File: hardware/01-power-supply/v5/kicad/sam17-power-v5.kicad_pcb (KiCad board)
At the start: 2 copper layers, 200 x 150 mm, 161 parts, among them J1 KPJX-PM-4S, J10 PinHeader 1x04 P2.54mm, J2 Molex KK-254 4 pos (con llave), J5 Faston 6.3x0.8 PCB, J6 Molex KK-254 2 pos, J8 PinHeader 1x04 P2.54mm, J9 Molex KK-254 2 pos, Q2 N-MOSFET 60V 40A Ron<5mohm, SW1 Pulsador tactil 6x6mm THT, U1 Linear Tech LT1963AEST#TRPBF, U10 TI ADS1115IDGSR, U11 TI TMP1075DGKR, U12 TI INA226AIDGSR, U13 TI INA226AIDGSR, U14 TI INA226AIDGSR, U15 TI LM74502DDFR, U16 TI TPS26630PWPR, U17 TI MSP430FR2111IPW16, U18 TI TPS70933DBVR, U19 TI TPS26630PWPR, U2 Linear Tech LT3015EQ#TRPBF, U20 TI LM393BDR, U21 TI TL431BIDBZR, U22 TI TL431BIDBZR, U23 TI TL431BIDBZR, U24 TI TL431BIDBZR, U25 TI TL431BIDBZR, U4 Linear Tech LT3045EDD#TRPBF, U5 Linear Tech LT3045EDD#TRPBF, U6 Linear Tech LT3094EDD#PBF, U7 Linear Tech LT3094EDD#PBF, U8 TI INA226AIDGSR, U9 TI ISO1541D

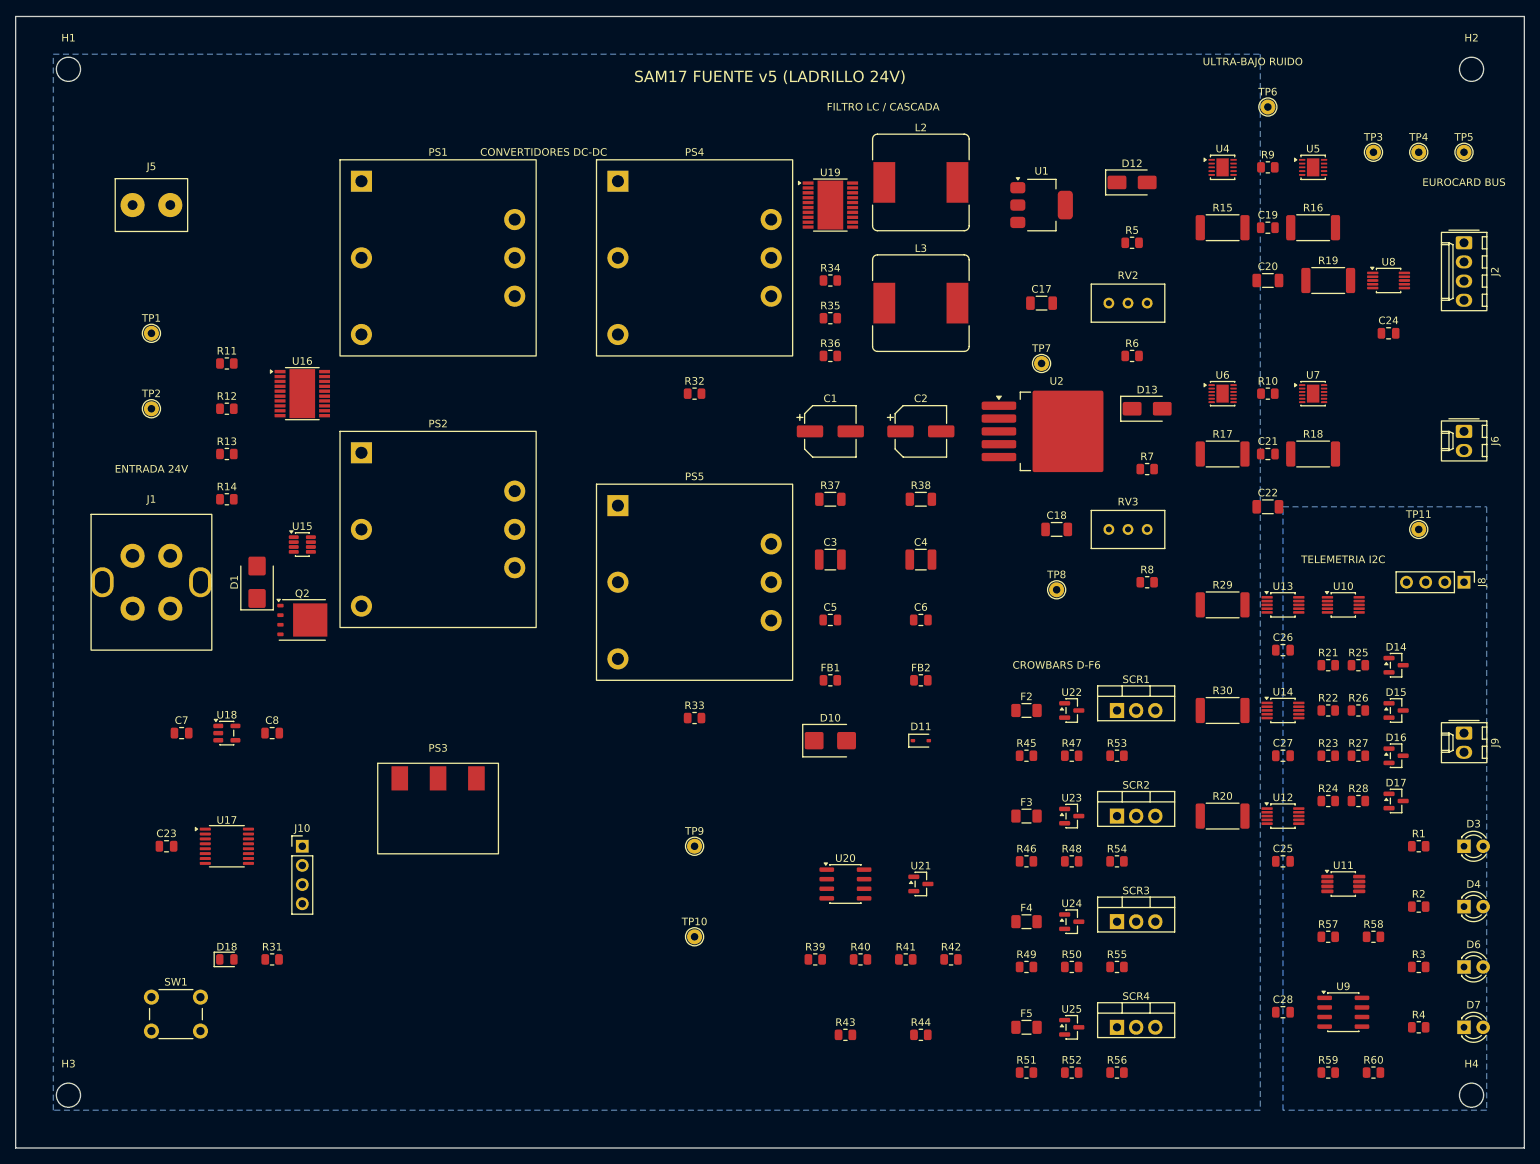
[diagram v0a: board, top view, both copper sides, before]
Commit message: hardware: fuente v5, placa ruteada con DRC en cero y paquete de fabricacion
La placa anterior no tenia ni una pista (161 huellas, 0 segmentos, 0
vias) y fab/README.md decia "ruteada y con DRC en cero". Esta sale
entera de build_pcb.py desde el netlist:

- 200 x 150 mm, 4 capas: F.Cu | In1 masas GND24/GNDA/GNDD | In2 | B.Cu.
  GNDD queda a >= 2 mm de las otras dos en las cuatro capas; GND24 y
  GNDA solo se tocan en NT1, en los pads de masa de PS3.
- Los caminos de ~3 A (24 V de entrada y +5 V digital) van en cobre
  fijo de >= 1,4 mm, no en pista ruteada. Cobre y 36 vias termicas para
  U1 y otras 36 para U2. 105 vias de masa cosidas antes de rutear.
- Freerouting 2.4.1 por linea de ordenes (la mejor de 3 rondas) y
  rescate.py, un A* propio, para las conexiones que deja abiertas (6).
- DRC de kicad-cli con todas las severidades, zonas rellenas y paridad
  con el esquematico: 0 infracciones, 0 sin conectar, 0 de paridad.
  1331 pistas y 274 vias.

Dos trampas de pcbnew 10:
- SaveBoard reconstruye la conectividad y PROPAGA redes: las 36 vias
  termicas de U2 (-15V5_FILT) tocaban el relleno viejo de GNDA en In1 y
  se guardaban en GNDA. Se vacian los rellenos antes del cobre termico.
- board.Remove() le pasa la propiedad a Python y SWIG, sin destructor,
  corrompe lo que se crea despues ("SwigPyObject ... NewOutline").
  quitar() deja el objeto quitado sin dueno.

Puertas:
- check_pcb.py, en Python pelado (corre tambien en CI): paridad pad a
  pad con el netlist, evidencia de DRC atada al sha256 de la placa,
  caminos de 3 A, huecos entre masas y vias termicas. --mutar pone 6
  canarios; uno es el de las vias de U2 en GNDA.
- check_drc.py repite el DRC en vivo donde hay kicad-cli.
- check_fab.py reexporta con las ordenes de build_fab.py y compara.

Fabricacion: build_fab.py escribe los 10 gerbers, el taladro, las
posiciones, el BOM y el CPL de JLC (bom_jlc.py decide por la placa) y
las vistas de pcb/. El esquematico va con etiquetas globales para que
la paridad del DR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
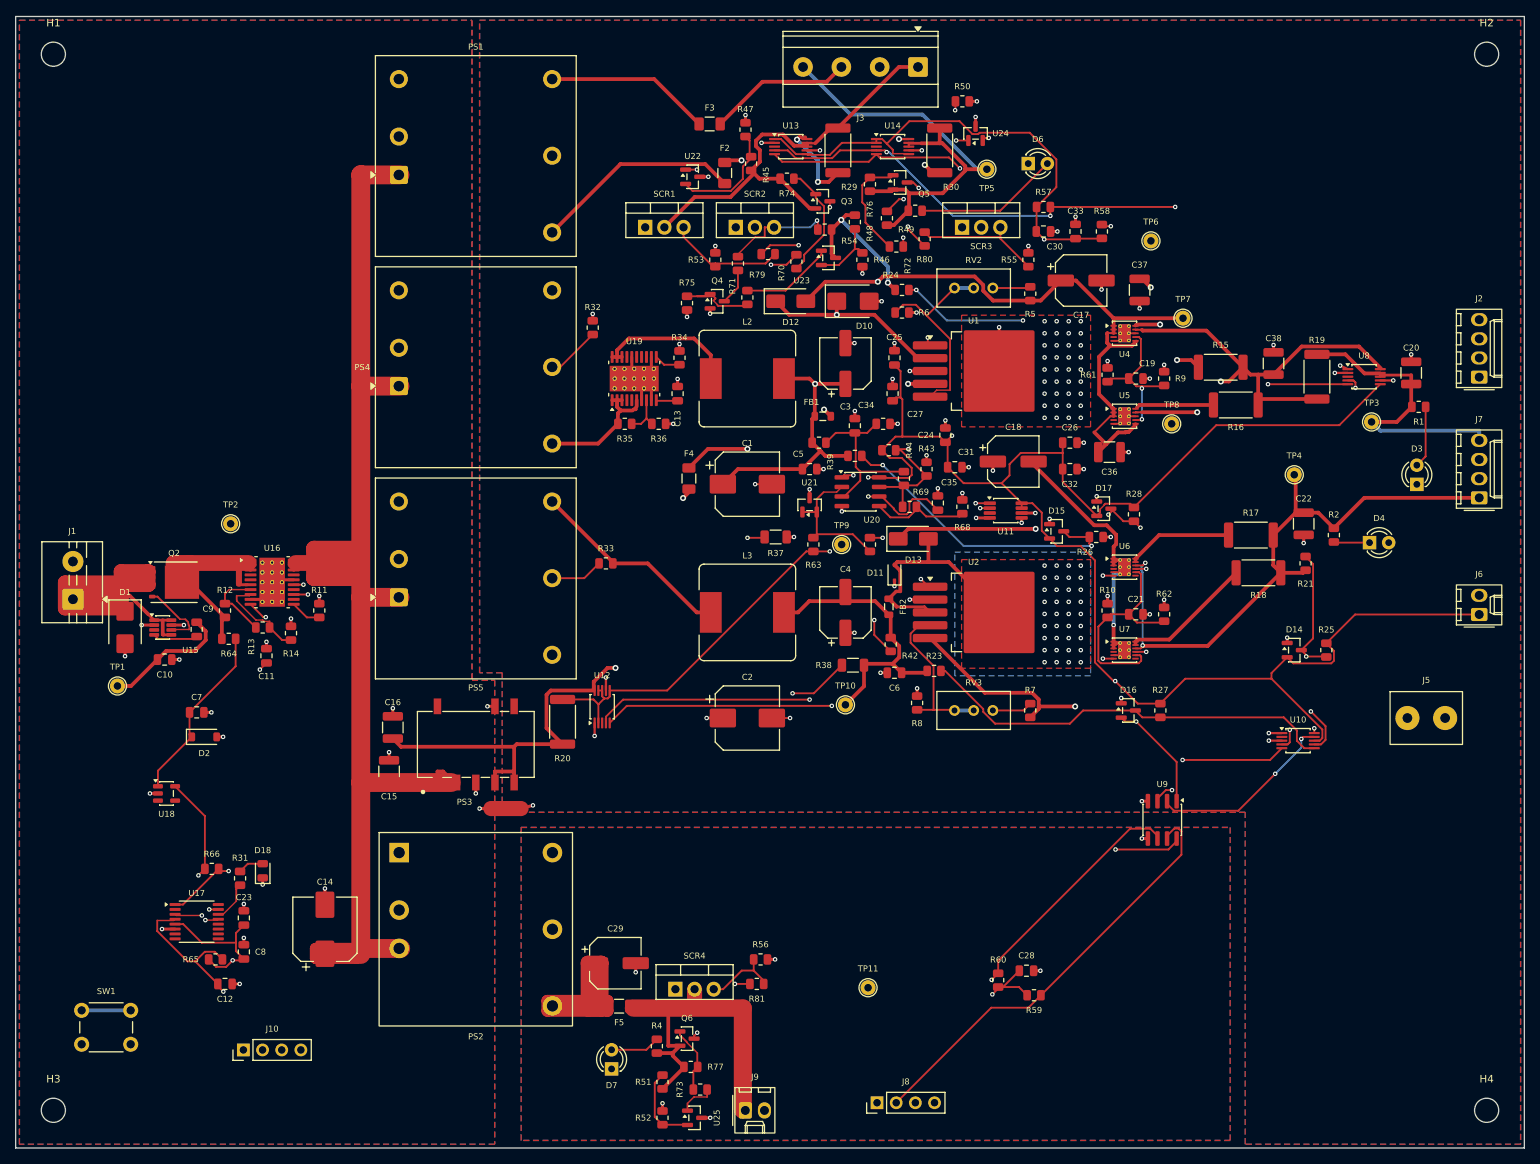
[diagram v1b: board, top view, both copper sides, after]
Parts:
- added C10: 100nF 50V X7R, Capacitor_SMD:C_0805_2012Metric, F.Cu at (19.8, 85.2)
- added C11: 22nF 50V X7R, Capacitor_SMD:C_0805_2012Metric, F.Cu at (33.2, 84.8)
- added C12: 1nF 50V C0G, Capacitor_SMD:C_0805_2012Metric, F.Cu at (27.8, 128.2)
- added C13: 22nF 50V X7R, Capacitor_SMD:C_0805_2012Metric, F.Cu at (87.8, 50.0)
- added C14: 100uF 50V, Capacitor_SMD:CP_Elec_8x10, F.Cu at (41.0, 121.0)
- added C15: 10uF 50V X7R, Capacitor_SMD:C_1210_3225Metric, F.Cu at (49.5, 100.1)
- added C16: 22uF 25V X7R, Capacitor_SMD:C_1210_3225Metric, F.Cu at (50.0, 94.2)
- added C29: 100uF 25V, Capacitor_SMD:CP_Elec_6.3x7.7, F.Cu at (79.5, 125.5)
- added C30: 100nF 50V X7R, Capacitor_SMD:C_0805_2012Metric, F.Cu at (136.2, 28.5)
- added C31: 100nF 50V X7R, Capacitor_SMD:C_0805_2012Metric, F.Cu at (124.5, 59.8)
- added C32: 100nF 50V X7R, Capacitor_SMD:C_0805_2012Metric, F.Cu at (139.8, 60.0)
- added C33: 100nF 50V X7R, Capacitor_SMD:C_0805_2012Metric, F.Cu at (140.5, 28.5)
- added C34: 100nF 50V X7R, Capacitor_SMD:C_0805_2012Metric, F.Cu at (111.2, 54.2)
- added C35: 100nF 50V X7R, Capacitor_SMD:C_0805_2012Metric, F.Cu at (122.2, 64.5)
- added C36: 22uF 25V X7R, Capacitor_SMD:C_1210_3225Metric, F.Cu at (145.0, 57.8)
- added C37: 22uF 25V X7R, Capacitor_SMD:C_1210_3225Metric, F.Cu at (149.0, 36.2)
- added C38: 22uF 25V X7R, Capacitor_SMD:C_1210_3225Metric, F.Cu at (166.8, 46.0)
- added C9: 100nF 50V X7R, Capacitor_SMD:C_0805_2012Metric, F.Cu at (24.0, 81.2)
- added D2: BZT52C30, Diode_SMD:D_SOD-123, F.Cu at (25.0, 95.5)
- added J3: Bornera 4P 5.08 mm, TerminalBlock_Phoenix:TerminalBlock_Phoenix_MKDS-1,5-4-5.08_1x04_P5.08mm_Horizontal, F.Cu at (119.6, 6.70)
- added J7: Molex KK-254 4P, Connector_Molex:Molex_KK-254_AE-6410-04A_1x04_P2.54mm_Vertical, F.Cu at (194.0, 63.8)
- added NT1: NetTie GND24-GNDA, NetTie:NetTie-2_SMD_Pad2.0mm, F.Cu at (65.0, 105.0)
- added Q3: MMBT3906, Package_TO_SOT_SMD:SOT-23, F.Cu at (107.0, 24.5)
- added Q4: MMBT3906, Package_TO_SOT_SMD:SOT-23, F.Cu at (93.0, 37.8)
- added Q5: MMBT3906, Package_TO_SOT_SMD:SOT-23, F.Cu at (117.2, 22.0)
- added Q6: MMBT3906, Package_TO_SOT_SMD:SOT-23, F.Cu at (89.0, 135.5)
- added R61: 120k 0.1%, Resistor_SMD:R_0805_2012Metric, F.Cu at (144.8, 47.5)
- added R62: 120k 0.1%, Resistor_SMD:R_0805_2012Metric, F.Cu at (152.2, 79.2)
- added R63: 1.2k, Resistor_SMD:R_0805_2012Metric, F.Cu at (105.8, 70.0)
- added R64: 220, Resistor_SMD:R_0805_2012Metric, F.Cu at (28.2, 82.5)
- added R65: 47k, Resistor_SMD:R_0805_2012Metric, F.Cu at (26.5, 125.0)
- added R66: 10k, Resistor_SMD:R_0805_2012Metric, F.Cu at (26.0, 113.0)
- added R67: 6.8M, Resistor_SMD:R_0805_2012Metric, F.Cu at (117.8, 61.2)
- added R68: 10k, Resistor_SMD:R_0805_2012Metric, F.Cu at (125.5, 65.0)
- added R69: 10M, Resistor_SMD:R_0805_2012Metric, F.Cu at (118.5, 65.0)
- added R70: 1k, Resistor_SMD:R_0805_2012Metric, F.Cu at (103.5, 32.5)
- added R71: 1k, Resistor_SMD:R_0805_2012Metric, F.Cu at (97.0, 37.2)
- added R72: 1k, Resistor_SMD:R_0805_2012Metric, F.Cu at (116.8, 30.5)
- added R73: 1k, Resistor_SMD:R_0805_2012Metric, F.Cu at (90.8, 142.2)
- added R74: 10k, Resistor_SMD:R_0805_2012Metric, F.Cu at (102.2, 21.5)
- added R75: 10k, Resistor_SMD:R_0805_2012Metric, F.Cu at (89.0, 38.0)
- added R76: 10k, Resistor_SMD:R_0805_2012Metric, F.Cu at (113.2, 22.2)
- added R77: 10k, Resistor_SMD:R_0805_2012Metric, F.Cu at (89.5, 139.2)
- added R78: 100, Resistor_SMD:R_0805_2012Metric, F.Cu at (99.8, 31.5)
- added R79: 100, Resistor_SMD:R_0805_2012Metric, F.Cu at (95.8, 32.8)
- added R80: 100, Resistor_SMD:R_0805_2012Metric, F.Cu at (120.5, 29.5)
- added R81: 100, Resistor_SMD:R_0805_2012Metric, F.Cu at (98.2, 128.2)
- C1, C2: value 47uF 25V electrolitico SMD -> 220uF 35V; footprint CP_Elec_6.3x7.7 -> Capacitor_SMD:CP_Elec_8x10
- C17, C18: value 10uF 25V X7R 1206 -> 47uF 35V; footprint C_1206_3216Metric -> Capacitor_SMD:CP_Elec_6.3x7.7
- C19, C21: value 470nF 25V X7R 0805 -> 470nF 50V X7R; footprint C_0805_2012Metric -> Capacitor_SMD:C_0805_2012Metric
- C20, C22: value 10uF 25V X7R 1206 -> 22uF 25V X7R; footprint C_1206_3216Metric -> Capacitor_SMD:C_1210_3225Metric
- C23, C24, C25, C26, C27, C28, C5, C6: value 100nF 50V X7R 0805 -> 100nF 50V X7R; footprint C_0805_2012Metric -> Capacitor_SMD:C_0805_2012Metric
- C3, C4: value 22uF 25V X7R 1210 -> 47uF 35V; footprint C_1210_3225Metric -> Capacitor_SMD:CP_Elec_6.3x7.7
- C7: value 1uF 50V X7R 0805 -> 1uF 50V X7R; footprint C_0805_2012Metric -> Capacitor_SMD:C_0805_2012Metric
- C8: value 1uF 50V X7R 0805 -> 4.7uF 25V X7R; footprint C_0805_2012Metric -> Capacitor_SMD:C_0805_2012Metric
- D1: value Bourns SMBJ26A TVS -> SMBJ26CA; footprint D_SMB -> Diode_SMD:D_SMB
- D10: value Bourns SMBJ16A TVS -> SMBJ16A; footprint D_SMB -> Diode_SMD:D_SMB
- D11: value Schottky BAT54WS 30V 200mA -> BAT54WS; footprint D_SOD-323 -> Diode_SMD:D_SOD-323
- D12, D13: value 1N4001 / S1M -> S1M; footprint D_SMA -> Diode_SMD:D_SMA
- D14, D15, D16, D17: value Diodo Schottky doble BAT54S -> BAT54S; footprint SOT-23 -> Package_TO_SOT_SMD:SOT-23
- D18: value LED azul 0805 -> LED verde 0805; footprint LED_0805_2012Metric -> LED_SMD:LED_0805_2012Metric
- D3, D4, D6, D7: footprint LED_D3.0mm -> LED_THT:LED_D3.0mm
- F2, F3: value Bourns SF-1206F300-2 3.0A Fast Blow -> SF-1206F300-2 3A; footprint Fuse_1206_3216Metric -> Fuse:Fuse_1206_3216Metric
- F4: value Bourns SF-1206F200-2 2.0A Fast Blow -> SF-1206F200-2 2A; footprint Fuse_1206_3216Metric -> Fuse:Fuse_1206_3216Metric
- F5: value Bourns SF-1206F400-2 4.0A Fast Blow -> 0466004 4A; footprint Fuse_1206_3216Metric -> Fuse:Fuse_1206_3216Metric
- FB1, FB2: value Ferrita 60 ohm @ 100MHz 2A -> BLM21PG600SN1D; footprint R_0805_2012Metric -> Inductor_SMD:L_0805_2012Metric
- H1, H2, H3, H4: footprint MountingHole_3.2mm_M3 -> MountingHole:MountingHole_3.2mm_M3
- J1: value KPJX-PM-4S -> Bornera 2P 5.0 mm; footprint Kycon_KPJX-PM-4S -> TerminalBlock:TerminalBlock_MaiXu_MX126-5.0-02P_1x02_P5.00mm
- J10, J8: value PinHeader 1x04 P2.54mm -> PinHeader 1x04; footprint PinHeader_1x04_P2.54mm_Vertical -> Connector_PinHeader_2.54mm:PinHeader_1x04_P2.54mm_Vertical
- J2: value Molex KK-254 4 pos (con llave) -> Molex KK-254 4P; footprint Molex_KK-254_AE-6410-04A_1x04_P2.54mm_Vertical -> Connector_Molex:Molex_KK-254_AE-6410-04A_1x04_P2.54mm_Vertical
- J5: footprint Faston_6.3x0.8mm_PCB_2Leg_P5.0mm -> sam17:Faston_6.3x0.8mm_PCB_2Leg_P5.0mm
- J6, J9: value Molex KK-254 2 pos -> Molex KK-254 2P; footprint Molex_KK-254_AE-6410-02A_1x02_P2.54mm_Vertical -> Connector_Molex:Molex_KK-254_AE-6410-02A_1x02_P2.54mm_Vertical
- L2, L3: value 10uH 2.5A DCR<35mohm -> 22uH SRR1260-220M; footprint L_Bourns_SRR1260 -> Inductor_SMD:L_Bourns_SRR1260
- PS1: value TRACO THN 30-2422WI -> THN 30-2422WI; footprint Converter_DCDC_TRACO_THN-30WI_THT -> Converter_DCDC:Converter_DCDC_TRACO_THL30-xxxxWI_THT
- PS2: value Mornsun URB2405YMD-20WR3 -> URB2405YMD-20WR3; footprint Converter_DCDC_Mornsun_URB-YMD-20WR3_THT -> sam17:Converter_DCDC_Mornsun_URB_YMD-20WR3_Horizontal_THT
- PS3: value Mornsun K7805T-1000R3 -> K7805T-1000R3; footprint Converter_DCDC_Mornsun_K78_T1000R3_SMD -> sam17:Converter_DCDC_Mornsun_K78_T-1000R3_SMD
- PS4, PS5: value TRACO THN 20-2413WI -> THN 20-2413WI; footprint Converter_DCDC_TRACO_THN-20WI_THT -> Converter_DCDC:Converter_DCDC_TRACO_THL30-xxxxWI_THT
- Q2: value N-MOSFET 60V 40A Ron<5mohm -> CSD18534Q5A; footprint TDSON-8-1 -> Package_TO_SOT_SMD:TDSON-8-1
- R1, R2: value 2.2k 1/4W 0805 -> 2.2k; footprint R_0805_2012Metric -> Resistor_SMD:R_0805_2012Metric
- R10, R9: value 120k 0.1% 25ppm 0805 -> 120k 0.1%; footprint R_0805_2012Metric -> Resistor_SMD:R_0805_2012Metric
- R11: value 4.02k 1% 0805 -> 4.02k; footprint R_0805_2012Metric -> Resistor_SMD:R_0805_2012Metric
- R12, R35: value 49.9k 0.1% 0805 -> 49.9k 0.1%; footprint R_0805_2012Metric -> Resistor_SMD:R_0805_2012Metric
- R13: value 3.32k 0.1% 0805 -> 1.62k 0.1%; footprint R_0805_2012Metric -> Resistor_SMD:R_0805_2012Metric
- R14: value 2.00k 0.1% 0805 -> 1.96k 0.1%; footprint R_0805_2012Metric -> Resistor_SMD:R_0805_2012Metric
- R15, R16, R17, R18, R19, R29, R30: value 20 mohm 1% 1W 2512 -> 0.02; footprint R_2512_6332Metric -> Resistor_SMD:R_2512_6332Metric
- R20: value 100 mohm 1% 1W 2512 -> 0.1; footprint R_2512_6332Metric -> Resistor_SMD:R_2512_6332Metric
- R21, R22, R23, R24: value 100k 0.1% 0805 -> 100k 0.1%; footprint R_0805_2012Metric -> Resistor_SMD:R_0805_2012Metric
- R25, R26, R27, R28: value 20.0k 0.1% 0805 -> 20.0k 0.1%; footprint R_0805_2012Metric -> Resistor_SMD:R_0805_2012Metric
- R3, R4: value 680R 1/4W 0805 -> 680; footprint R_0805_2012Metric -> Resistor_SMD:R_0805_2012Metric
- R31: value 1.0k 1% 0805 -> 220; footprint R_0805_2012Metric -> Resistor_SMD:R_0805_2012Metric
- R32, R33: value 240k 1% 0805 -> 45.3k; footprint R_0805_2012Metric -> Resistor_SMD:R_0805_2012Metric
- R34: value 18.2k 1% 0805 -> 18.2k; footprint R_0805_2012Metric -> Resistor_SMD:R_0805_2012Metric
- R36: value 3.83k 0.1% 0805 -> 3.9k 0.1%; footprint R_0805_2012Metric -> Resistor_SMD:R_0805_2012Metric
- R37, R38: value 0.5 ohm 1% 1206 -> 0.68; footprint R_1206_3216Metric -> Resistor_SMD:R_1206_3216Metric
- R39: value 49.9k 0.1% 0805 -> 47.5k 0.1%; footprint R_0805_2012Metric -> Resistor_SMD:R_0805_2012Metric
- R40, R47, R48, R50, R52: value 10.0k 0.1% 0805 -> 10.0k 0.1%; footprint R_0805_2012Metric -> Resistor_SMD:R_0805_2012Metric
- R41: value 49.9k 0.1% 0805 -> 10.2k 0.1%; footprint R_0805_2012Metric -> Resistor_SMD:R_0805_2012Metric
- R42: value 10.0k 0.1% 0805 -> 59.0k 0.1%; footprint R_0805_2012Metric -> Resistor_SMD:R_0805_2012Metric
- R43: value 100k 1% 0805 -> 100k; footprint R_0805_2012Metric -> Resistor_SMD:R_0805_2012Metric
- R44: value 10.0k 1% 0805 -> 10k; footprint R_0805_2012Metric -> Resistor_SMD:R_0805_2012Metric
- R45, R46: value 45.3k 0.1% 0805 -> 45.3k 0.1%; footprint R_0805_2012Metric -> Resistor_SMD:R_0805_2012Metric
- R49: value 13.3k 0.1% 0805 -> 13.3k 0.1%; footprint R_0805_2012Metric -> Resistor_SMD:R_0805_2012Metric
- R5: value 8.66k 0.1% 0805 -> 9.31k 0.1%; footprint R_0805_2012Metric -> Resistor_SMD:R_0805_2012Metric
- R51: value 12.7k 0.1% 0805 -> 12.7k 0.1%; footprint R_0805_2012Metric -> Resistor_SMD:R_0805_2012Metric
- R53, R54, R55, R56: value 1.0k 1% 0805 -> 1k; footprint R_0805_2012Metric -> Resistor_SMD:R_0805_2012Metric
- R57, R58, R59, R60: value 2.2k 1% 0805 -> 2.2k; footprint R_0805_2012Metric -> Resistor_SMD:R_0805_2012Metric
- R6, R8: value 1.00k 0.1% 0805 -> 1.00k 0.1%; footprint R_0805_2012Metric -> Resistor_SMD:R_0805_2012Metric
- R7: value 9.09k 0.1% 0805 -> 9.09k 0.1%; footprint R_0805_2012Metric -> Resistor_SMD:R_0805_2012Metric
- RV2, RV3: value Bourns 3296W-1-102 (1k trimmer) -> 1k 3296W; footprint Potentiometer_Bourns_3296W_Vertical -> Potentiometer_THT:Potentiometer_Bourns_3296W_Vertical
- SCR1, SCR2, SCR3, SCR4: value NXP BT151-500R Tiristor TO-220 -> BT151-500R; footprint TO-220-3_Vertical -> Package_TO_SOT_THT:TO-220-3_Vertical
- SW1: value Pulsador tactil 6x6mm THT -> Pulsador 6x6; footprint SW_PUSH_6mm -> Button_Switch_THT:SW_PUSH_6mm
- TP1, TP10, TP11, TP2, TP3, TP4, TP5, TP6, TP7, TP8, TP9: value TestPoint Pad D2.0mm -> TestPoint; footprint TestPoint_THTPad_D2.0mm_Drill1.0mm -> TestPoint:TestPoint_THTPad_D2.0mm_Drill1.0mm
- U1: value Linear Tech LT1963AEST#TRPBF -> LT1963AEQ; footprint SOT-223-3_TabPin2 -> Package_TO_SOT_SMD:TO-263-5_TabPin3
- U10: value TI ADS1115IDGSR -> ADS1115IDGS; footprint MSOP-10_3x3mm_P0.5mm -> Package_SO:TSSOP-10_3x3mm_P0.5mm
- U11: value TI TMP1075DGKR -> TMP1075DGK; footprint VSSOP-8_3x3mm_P0.65mm -> Package_SO:VSSOP-8_3x3mm_P0.65mm
- U12, U13, U14, U8: value TI INA226AIDGSR -> INA226; footprint MSOP-10_3x3mm_P0.5mm -> Package_SO:TSSOP-10_3x3mm_P0.5mm
- U15: value TI LM74502DDFR -> LM74502DDFR; footprint SOT-23-8 -> Package_TO_SOT_SMD:SOT-23-8
- U16, U19: value TI TPS26630PWPR -> TPS26631PWPR; footprint HTSSOP-20-1EP_4.4x6.5mm_P0.65mm_EP3.4x6.5mm -> Package_SO:HTSSOP-20-1EP_4.4x6.5mm_P0.65mm_EP3.4x6.5mm_Mask2.96x2.96mm_ThermalVias
- U17: value TI MSP430FR2111IPW16 -> MSP430FR2111IPW16; footprint TSSOP-16_4.4x5mm_P0.65mm -> Package_SO:TSSOP-16_4.4x5mm_P0.65mm
- U18: value TI TPS70933DBVR -> TPS70933DBVR; footprint SOT-23-5 -> Package_TO_SOT_SMD:SOT-23-5
- U2: value Linear Tech LT3015EQ#TRPBF -> LT3015EQ; footprint TO-263-5_TabPin3 -> Package_TO_SOT_SMD:TO-263-5_TabPin3
- U20: value TI LM393BDR -> LM393B; footprint SOIC-8_3.9x4.9mm_P1.27mm -> Package_SO:SOIC-8_3.9x4.9mm_P1.27mm
- U21, U22, U23, U24, U25: value TI TL431BIDBZR -> TL431BI; footprint SOT-23 -> Package_TO_SOT_SMD:SOT-23
- U4, U5: value Linear Tech LT3045EDD#TRPBF -> LT3045EDD; footprint DFN-10-1EP_3x3mm_P0.5mm_EP1.65x2.38mm -> Package_DFN_QFN:DFN-10-1EP_3x3mm_P0.5mm_EP1.65x2.38mm_ThermalVias
- U6, U7: value Linear Tech LT3094EDD#PBF -> LT3094EDD; footprint DFN-12-1EP_3x3mm_P0.45mm_EP1.65x2.38mm -> Package_DFN_QFN:DFN-12-1EP_3x3mm_P0.45mm_EP1.65x2.38mm_ThermalVias
- U9: value TI ISO1541D -> ISO1541; footprint SOIC-8_3.9x4.9mm_P1.27mm -> Package_SO:SOIC-8_3.9x4.9mm_P1.27mm
- moved J5 182.2 mm to (187.0, 93.0)
- moved D6 121.2 mm to (134.2, 19.5)
- moved R3 120.4 mm to (119.2, 25.8)
- moved R50 115.7 mm to (125.5, 11.2)
- moved D7 113.1 mm to (79.0, 139.5), turned to 90 degrees
- moved J9 107.6 mm to (96.7, 145.0), turned to 0 degrees
- moved U24 105.3 mm to (127.2, 15.5), turned to 90 degrees
- moved J8 104.0 mm to (114.2, 144.0), turned to 90 degrees
- moved R57 103.9 mm to (136.2, 25.2)
- moved R4 101.0 mm to (85.0, 136.5), turned to 90 degrees
- moved R49 101.0 mm to (115.5, 26.8), turned to 90 degrees
- moved F3 100.9 mm to (92.0, 14.2)
- moved R58 100.2 mm to (144.0, 28.5), turned to 90 degrees
- moved TP11 95.0 mm to (113.0, 128.8)
- moved R55 94.5 mm to (134.2, 32.2), turned to 90 degrees
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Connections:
- C7 pad 1: +24V_PROT -> +24V_LDO
- D14 pad 1: AIN0 -> GNDA
- D14 pad 3: GNDA -> AIN0
- D15 pad 1: AIN1 -> GNDA
- D15 pad 3: GNDA -> AIN1
- D16 pad 1: AIN2 -> GNDA
- D16 pad 3: GNDA -> AIN2
- D17 pad 1: AIN3 -> GNDA
- D17 pad 3: GNDA -> AIN3
- J1 pad 2: +24V_RAW -> GND24
- J6 pad 1: +5V_RACK -> +5V_AUX
- PS1 pad 3: unconnected-(PS1-REMOTE-Pad3) -> +12V_RAW_RACK
- PS1 pad 4: +12V_RAW_RACK -> GNDA
- PS1 pad 5: GNDA -> -12V_RAW_RACK
- PS1 pad 6: -12V_RAW_RACK -> unconnected-(PS1-Remote-Pad6)
- PS2 pad 1: +24V_SW -> unconnected-(PS2-Ctrl-Pad1)
- PS2 pad 3: unconnected-(PS2-CTRL-Pad3) -> +24V_SW
- PS2 pad 5: GNDD -> unconnected-(PS2-Trim-Pad5)
- PS2 pad 6: unconnected-(PS2-TRIM-Pad6) -> GNDD
- PS3 pad 2: GNDA -> +24V_SW
- PS3 pad 3: +5V_RAW_RACK -> GND24
- PS4 pad 3: unconnected-(PS4-REMOTE-Pad3) -> +15V5_RAW
- PS4 pad 4: +15V5_RAW -> TRIM_PS4
- PS4 pad 6: TRIM_PS4 -> unconnected-(PS4-Remote-Pad6)
- PS5 pad 3: unconnected-(PS5-REMOTE-Pad3) -> GNDA
- PS5 pad 4: GNDA -> TRIM_PS5
- PS5 pad 6: TRIM_PS5 -> unconnected-(PS5-Remote-Pad6)
- Q2 pad 1: (no net) -> +24V_RAW
- Q2 pad 2: (no net) -> +24V_RAW
- Q2 pad 3: (no net) -> +24V_RAW
- Q2 pad 4: (no net) -> GATE_Q2
- Q2 pad 5: (no net) -> +24V_PROT
- R13 pad 2: OVPR_U16 -> OVP_U16
- R14 pad 1: OVPR_U16 -> OVP_U16
- R32 pad 2: +15V5_RAW -> GNDA
- R35 pad 2: OVPR_U19 -> OVP_U19
- R36 pad 1: OVPR_U19 -> OVP_U19
- R41 pad 1: +5V_AUX -> VREF_2V5
- U13 pad 1: SDA_A -> +5V_AUX
- U14 pad 1: SDA_A -> +5V_AUX
- U15 pad 2: +24V_RAW -> GND24
- U15 pad 4: GATE_Q2 -> VCAP_U15
- U15 pad 5: +24V_PROT -> +24V_RAW
- U15 pad 6: GND24 -> GATE_Q2
- U15 pad 7: (no net) -> GND24
- U15 pad 8: (no net) -> +24V_RAW
- U16 pad 10: FLT_M5 -> DVDT_U16
- U16 pad 11: IMON_M5 -> ILIM_U16
- U16 pad 12: ILIM_U16 -> unconnected-(U16-MODE-Pad12)
- U16 pad 13: GND24 -> SHDN_M5
- U16 pad 14: (no net) -> unconnected-(U16-IMON-Pad14)
- U16 pad 15: +24V_SW -> FLT_M5
- U16 pad 16: (no net) -> GND24
- U16 pad 17: (no net) -> unconnected-(U16-PGOOD-Pad17)
- U16 pad 18: (no net) -> +24V_SW
- U16 pad 19: (no net) -> +24V_SW
- U16 pad 2: (no net) -> +24V_PROT
- U16 pad 20: (no net) -> +24V_SW
- U16 pad 21: (no net) -> GND24
- U16 pad 3: (no net) -> +24V_PROT
- U16 pad 4: UVLO_U16 -> unconnected-(U16-B_GATE-Pad4)
- U16 pad 5: OVPR_U16 -> unconnected-(U16-DRV-Pad5)
- U16 pad 6: GND24 -> +24V_PROT
- U16 pad 7: SHDN_M5 -> UVLO_U16
- U16 pad 8: GND24 -> OVP_U16
- U17 pad 1: unconnected-(U17-P1.0-Pad1) -> FLT_M5
- U17 pad 10: (no net) -> unconnected-(U17-P2.0-Pad10)
- U17 pad 11: MCU_RST -> unconnected-(U17-P1.7-Pad11)
- U17 pad 12: MCU_TEST -> unconnected-(U17-P1.6-Pad12)
- U17 pad 13: +3V3_MCU -> SW_RESET
- U17 pad 14: GND24 -> LED_CTRL
- U17 pad 15: (no net) -> SHDN_M5
- U17 pad 16: (no net) -> unconnected-(U17-P1.2-Pad16)
- U17 pad 2: FLT_M5 -> unconnected-(U17-P1.0-Pad2)
- U17 pad 3: unconnected-(U17-P1.2_OVP-Pad3) -> MCU_TEST
- U17 pad 4: SHDN_M5 -> MCU_RST
- U17 pad 5: LED_CTRL -> +3V3_MCU
- U17 pad 6: SW_RESET -> GND24
- U17 pad 9: (no net) -> unconnected-(U17-P2.1-Pad9)
- U18 pad 1: +24V_PROT -> +24V_LDO
- U18 pad 3: +24V_PROT -> unconnected-(U18-EN-Pad3)
- U19 pad 10: FLT_U19 -> DVDT_U19
- U19 pad 11: IMON_U19 -> ILIM_U19
- U19 pad 12: ILIM_U19 -> GNDA
- U19 pad 13: GNDA -> unconnected-(U19-~{SHDN}-Pad13)
- U19 pad 14: (no net) -> unconnected-(U19-IMON-Pad14)
- U19 pad 15: +15V5_EFUSE -> unconnected-(U19-~{FLT}-Pad15)
- U19 pad 16: (no net) -> GNDA
- U19 pad 17: (no net) -> unconnected-(U19-PGOOD-Pad17)
- U19 pad 18: (no net) -> +15V5_EFUSE
- U19 pad 19: (no net) -> +15V5_EFUSE
- U19 pad 2: (no net) -> +15V5_RAW
- U19 pad 20: (no net) -> +15V5_EFUSE
- U19 pad 21: (no net) -> GNDA
- U19 pad 3: (no net) -> +15V5_RAW
- U19 pad 4: +15V5_RAW -> unconnected-(U19-B_GATE-Pad4)
- U19 pad 5: OVPR_U19 -> unconnected-(U19-DRV-Pad5)
- U19 pad 6: GNDA -> +15V5_RAW
- U19 pad 7: SHDN_CASCADE -> GNDA
- U19 pad 8: GNDA -> OVP_U19
- U2 pad 2: -15V5_FILT -> GNDA
- U2 pad 3: GNDA -> -15V5_FILT
- U2 pad 4: -12V9 -> ADJ_U2
- U2 pad 5: ADJ_U2 -> -12V9
- U20 pad 5: SENSE_NEG -> REF0_NEG
- U20 pad 6: VREF_2V5 -> SENSE_NEG
- U21 pad 2: GNDA -> VREF_2V5
- U21 pad 3: VREF_2V5 -> GNDA
- U22 pad 1: REF_CB1 -> TLK_CB1
- U22 pad 2: GNDA -> REF_CB1
- U22 pad 3: GATE_SCR1 -> GNDA
- U23 pad 1: REF_CB2 -> TLK_CB2
- U23 pad 2: -12V_RACK -> REF_CB2
- U23 pad 3: GATE_SCR2 -> -12V_RACK
- U24 pad 1: REF_CB3 -> TLK_CB3
- U24 pad 2: GNDA -> REF_CB3
- U24 pad 3: GATE_SCR3 -> GNDA
- U25 pad 1: REF_CB4 -> TLK_CB4
- U25 pad 2: GNDD -> REF_CB4
- U25 pad 3: GATE_SCR4 -> GNDD
- U4 pad 6: GNDA -> +13V1
- U5 pad 6: GNDA -> +13V1
- U6 pad 5: GNDA -> -12V9
- U6 pad 7: GNDA -> unconnected-(U6-VIOC-Pad7)
- U7 pad 5: GNDA -> -12V9
- U7 pad 7: GNDA -> unconnected-(U7-VIOC-Pad7)
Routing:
- net +5V_AUX: track 0.00 -> 400.7 mm, vias 0 -> 6
- net SDA_A: track 0.00 -> 283.8 mm, vias 0 -> 8
- net SCL_A: track 0.00 -> 277.2 mm, vias 0 -> 7
- net +24V_SW: track 0.00 -> 187.9 mm
- net -12V9: track 0.00 -> 154.3 mm, vias 0 -> 4
- net GNDA: track 0.00 -> 108.9 mm, vias 0 -> 114
- net +13V1: track 0.00 -> 106.1 mm, vias 0 -> 2
- net AIN3: track 0.00 -> 99.4 mm, vias 0 -> 5
- net -12V_ULTRA: track 0.00 -> 98.5 mm, vias 0 -> 2
- net AIN1: track 0.00 -> 87.6 mm, vias 0 -> 3
- net +24V_RAW: track 0.00 -> 85.7 mm
- net +5V_RAW_RACK: track 0.00 -> 78.4 mm, vias 0 -> 2
- net -12V_RACK: track 0.00 -> 77.3 mm, vias 0 -> 2
- net +5V_RACK: track 0.00 -> 72.9 mm
- net OUTS_POS: track 0.00 -> 67.0 mm, vias 0 -> 2
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- added copper zone on B.Cu, net -15V5_FILT
- added copper zone on F.Cu, net -15V5_FILT
- added copper zone on In2.Cu, net -15V5_FILT
- added copper zone on B.Cu, net GND24
- added copper zone on F.Cu, net GND24
- added copper zone on In1.Cu, net GND24
- added copper zone on F.Cu, net GNDA
- added copper zone on In1.Cu, net GNDA
- added copper zone on F.Cu, net GNDD
- added copper zone on In1.Cu, net GNDD
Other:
- copper layers 2 -> 4
- board text added: "GND24"
- board text added: "GNDA"
- board text added: "GNDD (M1)"
- board text added: "SAM17 FUENTE v5-B (ladrillo 24 V)"
- board text removed: "CONVERTIDORES DC-DC"
- board text removed: "CROWBARS D-F6"
- board text removed: "ENTRADA 24V"
- board text removed: "EUROCARD BUS"
- board text removed: "FILTRO LC / CASCADA"
- board text removed: "SAM17 FUENTE v5 (LADRILLO 24V)"
- board text removed: "TELEMETRIA I2C"
- board text removed: "ULTRA-BAJO RUIDO"

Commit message: hardware: fuente v5, placa y fabricacion rehechas con el circuito nuevo
La placa sale de build_pcb.py sobre la netlist con R82-R84 y D19, y fab/ y
pcb/ de build_fab.py sobre esa placa:

- 1509 pistas y 285 vias (72 termicas de U1/U2, 107 de masa cosidas).
- Freerouting dejo 6 conexiones abiertas; rescate.py cerro las 6.
- DRC (kicad-cli 10.0.3, todas las severidades, zonas rellenas y paridad
  con el esquematico): 0 infracciones, 0 sin conectar, 0 de paridad.

Tres arreglos del generador:

- rescate.py: GetConnectedItems() devuelve las vias como PCB_TRACK, asi
  que isinstance(item, PCB_VIA) no las veia y _anclas() las trataba como
  una pista de largo cero. Su GetWidth() sin capa tumba el proceso en
  KiCad 10.0.3 (excepcion 0x80000003). Se distingue por GetClass().
- build_pcb.py, guardar(): en Windows SaveBoard escribe CRLF y git guarda
  el fichero en LF, asi que el sha256 de la evidencia del DRC no era el de
  la placa commiteada y check_pcb.py la daba por otra. La placa y el
  .kicad_pro se escriben en LF.
- build_pcb.py, COBRE: U4.9 (OUTS_POS) queda entre OUT_U4 y GNDA a 0,5 mm
  de paso, y Freerouting le cruzaba SET_POS por delante sin dejarle
  salida. Lleva una pista fija de 0,25 mm hacia fuera, como U16.6.

fab/README.md con las cifras nuevas; la disipacion de U1/U2 remite a
#478.
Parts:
- added D19: SS34, Diode_SMD:D_SMA, F.Cu at (82.8, 41.2)
- added R82: 6.8M, Resistor_SMD:R_0805_2012Metric, F.Cu at (77.0, 54.8)
- added R83: 47k, Resistor_SMD:R_0805_2012Metric, F.Cu at (31.8, 97.5)
- added R84: 10k, Resistor_SMD:R_0805_2012Metric, F.Cu at (33.2, 108.5)
- D2: value BZT52C30 -> BZT52C24
- R53, R54, R55, R56: value 1k -> 100
- R64: value 220 -> 1k
- moved C8 12.7 mm to (21.2, 115.0), turned to 0 degrees
- moved D18 9.66 mm to (34.5, 122.8)
- moved R31 7.81 mm to (30.8, 122.0), turned to 0 degrees
- moved R34 6.77 mm to (88.5, 38.5)
- moved R75 4.00 mm to (89.0, 34.0), turned to 0 degrees
- moved C23 1.77 mm to (30.0, 117.8)
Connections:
- U17 pad 16: unconnected-(U17-P1.2-Pad16) -> FLT_U19
- U19 pad 15: unconnected-(U19-~{FLT}-Pad15) -> FLT_U19
- U19 pad 7: GNDA -> UVLO_U19
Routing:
- net FLT_U19: track 0.00 -> 100.3 mm, vias 0 -> 3
- net -12V_RACK: track 77.3 -> 95.7 mm, vias 2 -> 1
- net +12V_ULTRA: track 57.8 -> 74.3 mm
- net OUT_U7: track 17.6 -> 30.1 mm
- net AIN3: track 99.4 -> 111.5 mm, vias 5 -> 3
- net SDA_A: track 283.8 -> 272.5 mm, vias 8 -> 9
- net SCL_A: track 277.2 -> 287.8 mm, vias 7 -> 9
- net +15V5_LC: track 59.4 -> 49.8 mm
- net OUT_U6: track 14.1 -> 23.3 mm
- net UVLO_U19: track 0.00 -> 9.17 mm, vias 0 -> 2
- net REF_CB3: track 25.6 -> 34.3 mm, vias 3 -> 2
- net +13V1: track 106.1 -> 113.8 mm, vias 2 -> 1
- net AIN0: track 30.7 -> 38.0 mm, vias 2 -> 0
- net +5V_RACK: track 72.9 -> 78.6 mm
- net +5V_FUSED_RACK: track 66.8 -> 61.1 mm, vias 3 -> 2
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
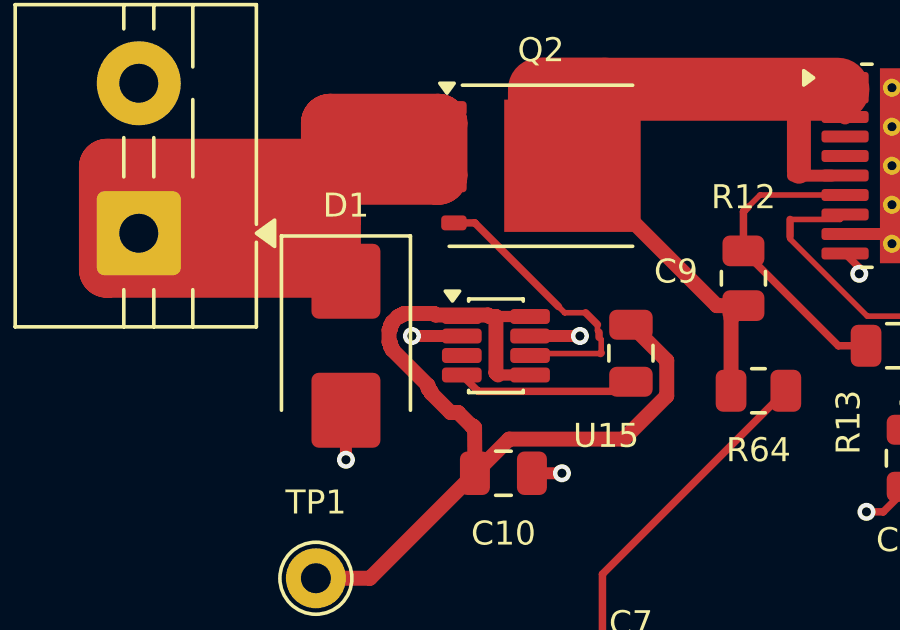
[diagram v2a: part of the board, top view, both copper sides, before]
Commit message: hardware: fuente v5, placa y fabricacion con R11 de 3,74 kOhm
build_pcb.py --desde-ruteo copia ahora tambien el valor de cada huella
desde el netlist, asi que un cambio de valor no pide otro Freerouting. La
placa sale del ruteo guardado de la corrida anterior:

- El cobre es el mismo salvo una conexion del rescate en +24V_RAW hasta
  U15.1, que pasa de 5 tramos a 2 (1506 pistas, 285 vias).
- DRC (kicad-cli 10.0.3, todas las severidades, zonas rellenas y paridad
  con el esquematico): 0 infracciones, 0 sin conectar, 0 de paridad.

lcsc_snapshot.csv entra C2960937 y sale C17663. Esquematico, netlist, fab/
y pcb/ regenerados.
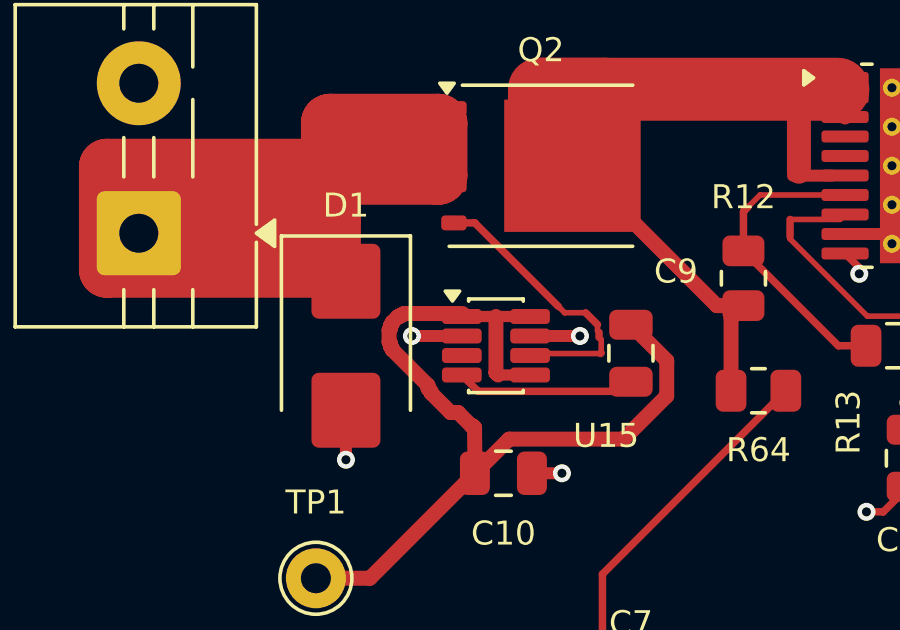
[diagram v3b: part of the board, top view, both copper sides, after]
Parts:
- R11: value 4.02k -> 3.74k
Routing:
- net +24V_RAW: track 87.8 -> 86.8 mm

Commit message: hardware: fuente v5, placa y fabricacion con R11 de vuelta en 4,02 kOhm
Desde el ruteo guardado, con build_pcb.py --desde-ruteo: el cobre es el de
la placa anterior, tramo a tramo (1506 pistas, 285 vias). DRC (kicad-cli
10.0.3, todas las severidades, zonas rellenas y paridad con el
esquematico): 0 infracciones, 0 sin conectar, 0 de paridad.

lcsc_snapshot.csv vuelve a C17663 y sale C2960937.
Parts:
- R11: value 3.74k -> 4.02k
